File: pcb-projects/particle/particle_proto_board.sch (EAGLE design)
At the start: 37 parts, among them IC1 ATTINY20-SOIC-14S1, IC2 DMC2400UV-SOT563, IC3 DMC2400UV-SOT563

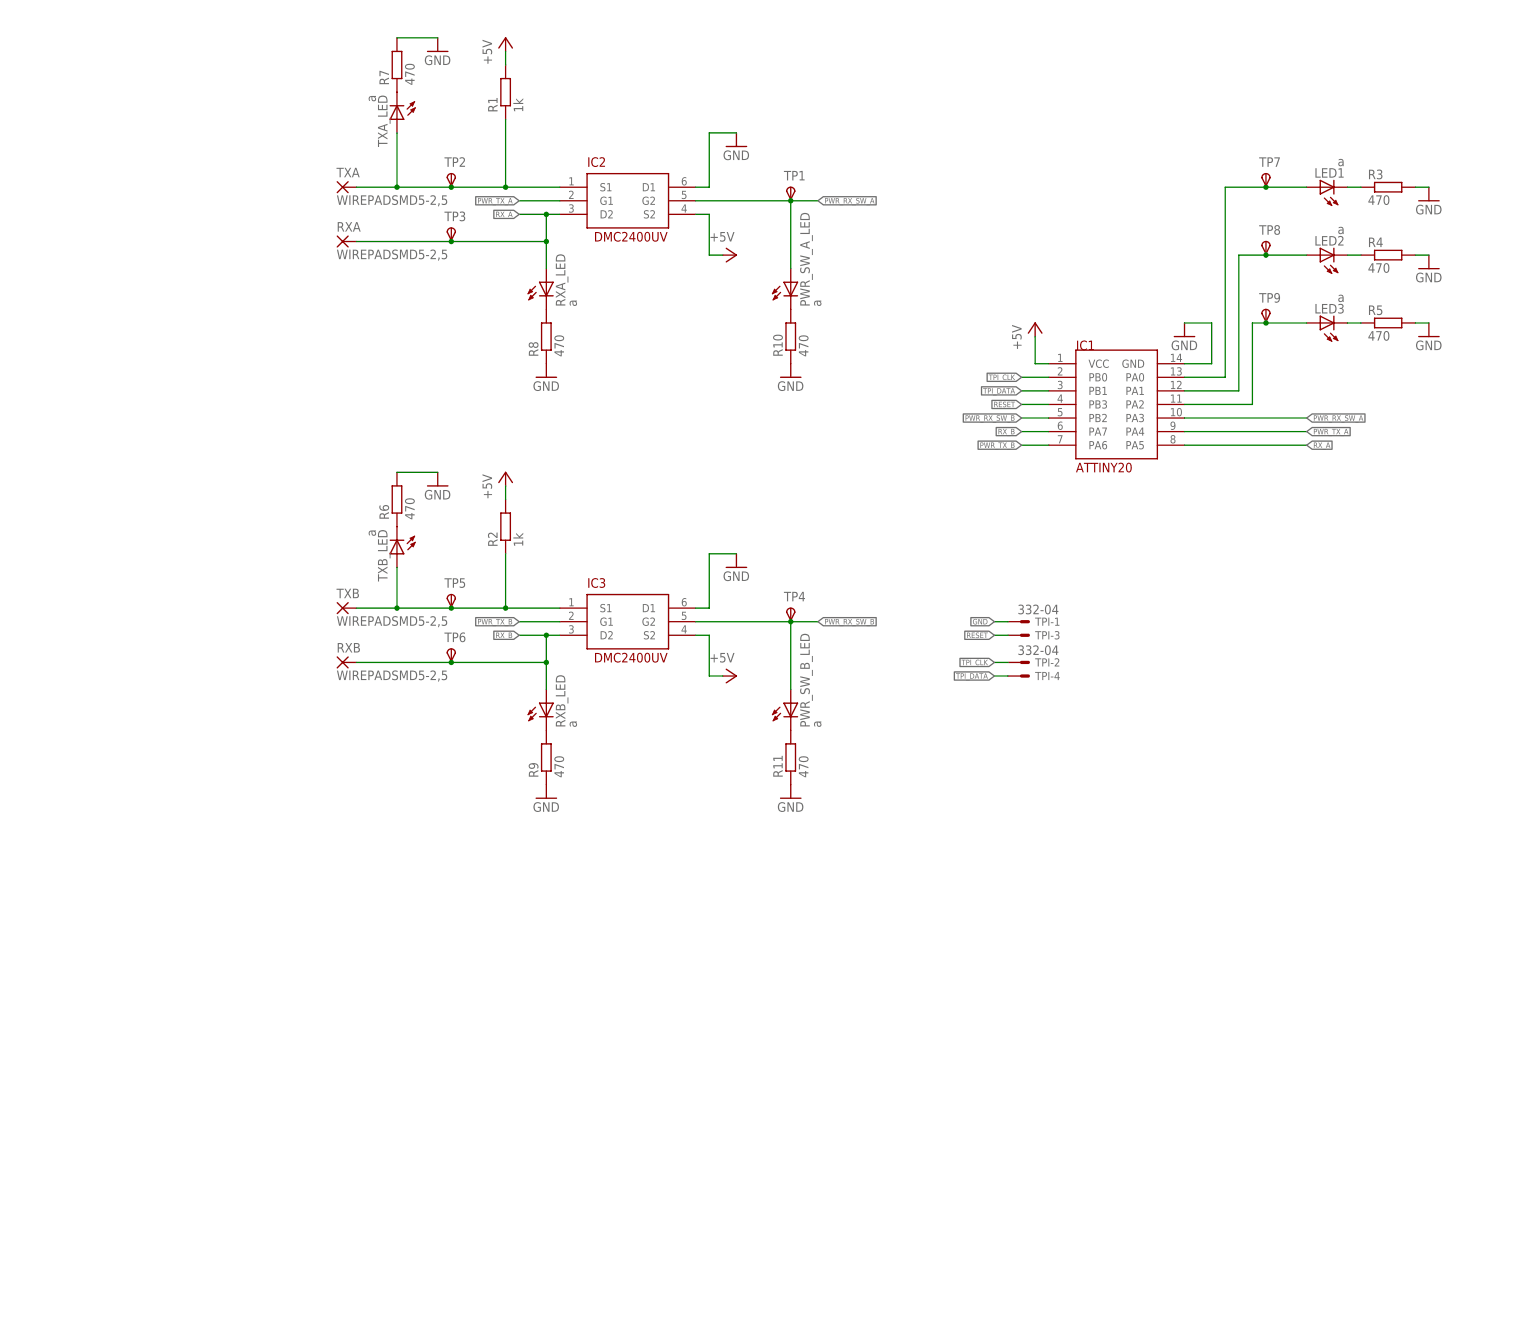
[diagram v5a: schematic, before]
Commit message: replaced packages/library of attiny20 and dmc2400uv
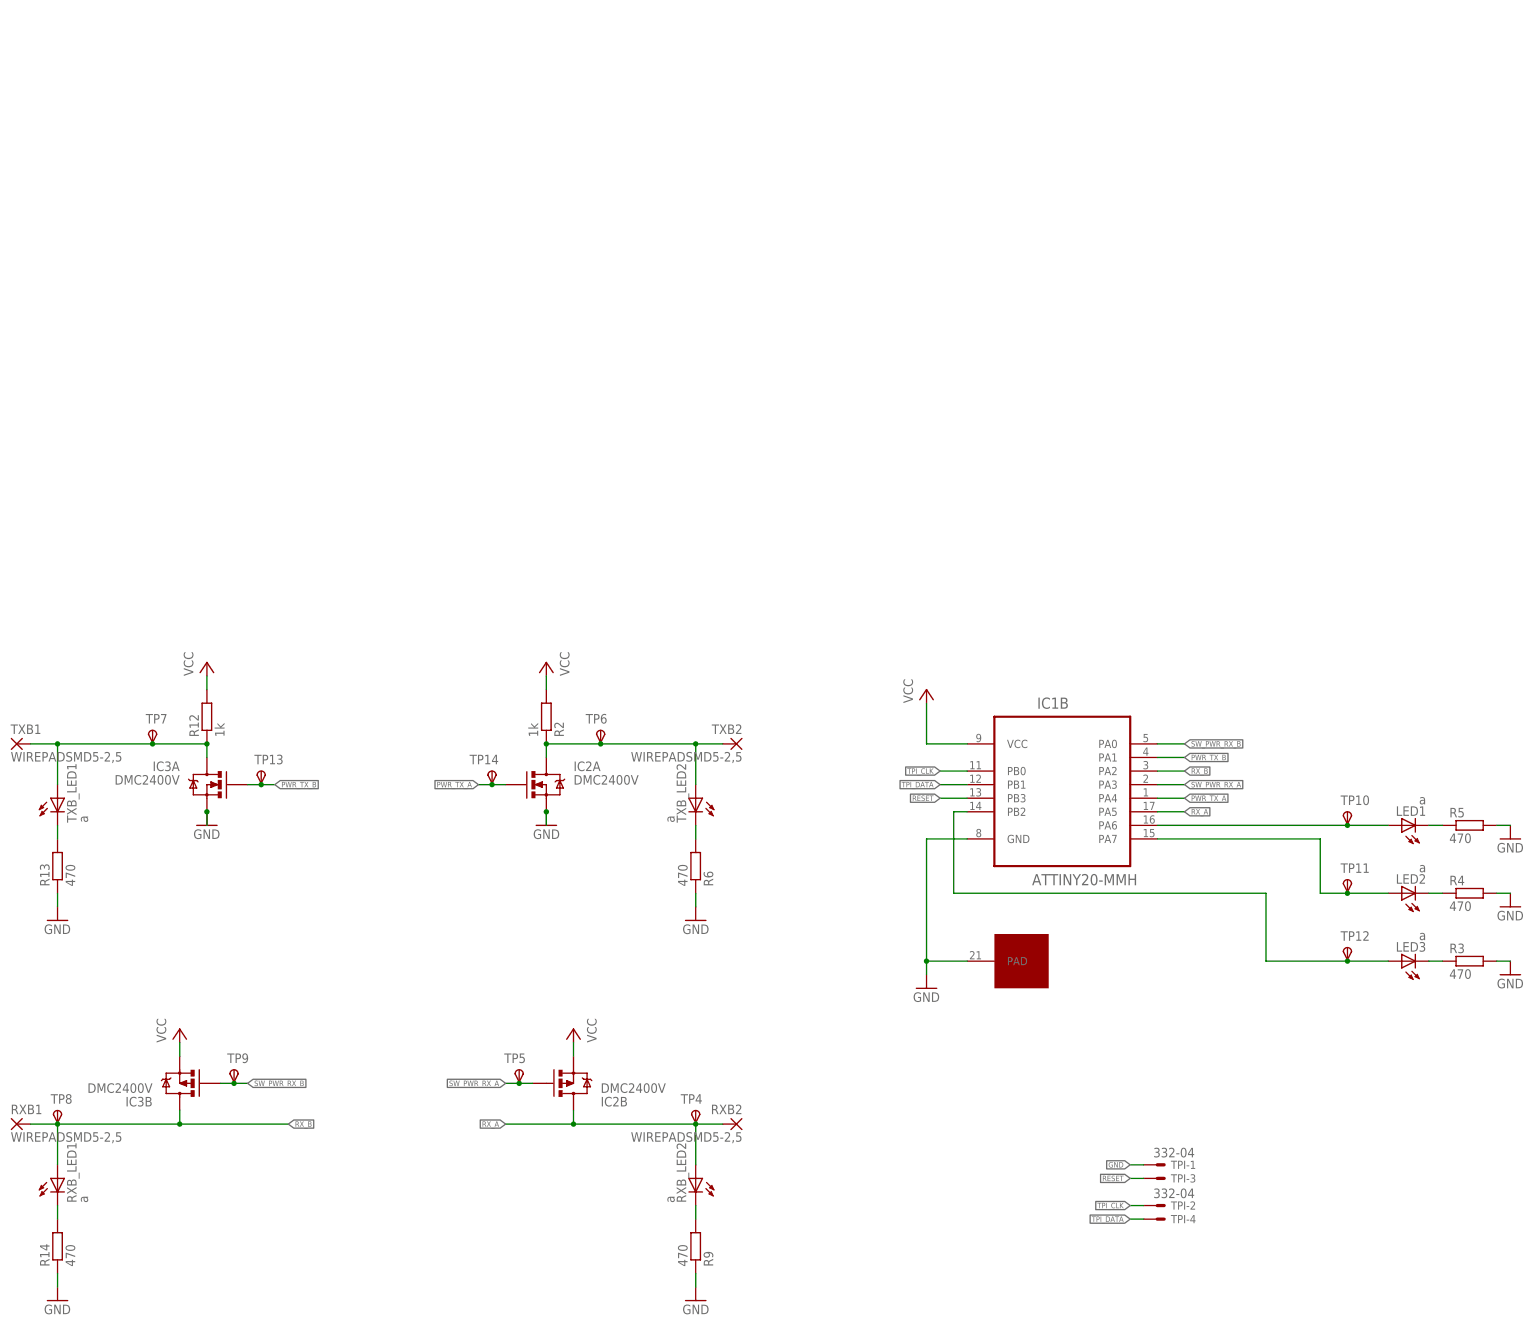
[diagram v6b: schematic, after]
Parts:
- removed PWR_SW_A_LED, PWR_SW_B_LED, RXA_LED, RXB_LED, TXA_LED, TXB_LED: a, led:LEDSML1206
- removed R1: 1k, rcl:R-EU_R1210
- removed R10, R11, R7, R8: 470, rcl:R-EU_R1210
- removed RXA, RXB, TXA, TXB: WIREPADSMD5-2,5, wirepad:WIREPADSMD5-2,5
- removed TP1, TP2, TP3: TPSPAD1-13, testpad:TPSPAD1-13
- added R12: 1k, rcl:R-EU_R1210
- added R13, R14: 470, rcl:R-EU_R1210
- added RXB1, RXB2, TXB1, TXB2: WIREPADSMD5-2,5, wirepad:WIREPADSMD5-2,5
- added RXB_LED1, RXB_LED2, TXB_LED1, TXB_LED2: a, led:LEDSML1206
- added TP10, TP11, TP12, TP13, TP14: TPSPAD1-13, testpad:TPSPAD1-13
- IC1: value ATTINY20-SOIC-14S1 -> ATTINY20-MMH; device ic-attiny20:ATTINY20-SOIC-14S1 -> tiny_particles_MCU:ATTINY20-MMH
- IC2, IC3: value DMC2400UV-SOT563 -> DMC2400V; device dmc2400uv:DMC2400UV-SOT563 -> diodes:DMC2400V
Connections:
- removed net +5V: IC1.VCC, IC2.S2, IC3.S2, R1.2, R2.2
- removed net N$11: R8.2, RXA_LED.C
- removed net N$12: R9.2, RXB_LED.C
- removed net N$13: PWR_SW_A_LED.C, R10.2
- removed net N$14: PWR_SW_B_LED.C, R11.2
- removed net N$5: R6.1, TXB_LED.C
- removed net N$7: R7.1, TXA_LED.C
- removed net PWR_RX_SW_A: IC1.PA3, IC2.G2, PWR_SW_A_LED.A, TP1.PP
- removed net PWR_RX_SW_B: IC1.PB2, IC3.G2, PWR_SW_B_LED.A, TP4.PP
- removed net PWR_TX_A_A_A: IC2.S1, R1.1, TP2.PP, TXA.P, TXA_LED.A
- removed net TXB: IC3.S1, R2.1, TP5.PP, TXB.P, TXB_LED.A
- new net N$21: IC1B.PA6, LED1.A, TP10.PP
- new net N$22: IC1B.PB2, LED3.A, TP12.PP
- new net N$23: IC1B.PA7, LED2.A, TP11.PP
- new net N$24: LED1.C, R5.1
- new net N$26: LED3.C, R3.1
- new net N$6: R13.2, TXB_LED1.C
- new net SW_PWR_RX_A: IC1B.PA3, IC2B.G, TP5.PP
- new net SW_PWR_RX_B: IC1B.PA0, IC3B.G, TP9.PP
- new net VCC: IC1B.VCC, IC2B.S, IC3B.S, R12.2, R2.2
- net GND: now also IC1A.PAD, IC1B.GND, IC2A.S, IC3A.S, R13.1, R14.1, R6.1; no longer IC1.GND, IC2.D1, IC3.D1, R10.1, R11.1, R6.2, R7.2, R8.1
- net N$1: now also IC3A.D, R12.1, TXB1.P, TXB_LED1.A; no longer IC1.PA0, LED1.A
- net N$2: now also IC2A.D, R2.1, TP6.PP, TXB2.P, TXB_LED2.A; no longer IC1.PA2, LED3.A, TP9.PP
- net N$3: now also R6.2, TXB_LED2.C; no longer IC1.PA1, LED2.A, TP8.PP
- net N$4: now also R9.2, RXB_LED2.C; no longer LED1.C, R3.1
- net N$8: now also R14.2, RXB_LED1.C; no longer LED3.C, R5.1
- net PWR_TX_A: now also IC1B.PA4, IC2A.G, TP14.PP; no longer IC1.PA4, IC2.G1
- net PWR_TX_B: now also IC1B.PA1, IC3A.G, TP13.PP; no longer IC1.PA6, IC3.G1
- net RESET: now also IC1B.PB3; no longer IC1.PB3
- net RX_A: now also IC1B.PA5, IC2B.D, RXB2.P, RXB_LED2.A, TP4.PP; no longer IC1.PA5, IC2.D2, RXA.P, RXA_LED.A, TP3.PP
- net RX_B: now also IC1B.PA2, IC3B.D, RXB1.P, RXB_LED1.A, TP8.PP; no longer IC1.PA7, IC3.D2, RXB.P, RXB_LED.A, TP6.PP
- net TPI_CLK: now also IC1B.PB0; no longer IC1.PB0
- net TPI_DATA: now also IC1B.PB1; no longer IC1.PB1
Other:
- moved on the sheet: LED1, LED2, LED3, R2, R3, R4, R5, R6, R9, TP4, TP5, TP6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

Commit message: close 21, close 22
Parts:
- added SPI: 332-06, con-garry:332-06
- TPI: value 332-04 -> 332-06; device con-garry:332-04 -> con-garry:332-06
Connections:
- removed net N$22: IC1B.PB2, LED3.A, TP12.PP
- removed net N$23: IC1B.PA7, LED2.A, TP11.PP
- removed net TPI_DATA: IC1B.PB1, TPI-4.S
- new net MISO: IC1B.PB2, LED3.A, SPI-1.S, TP12.PP
- new net SCK: IC1B.PA7, LED2.A, SPI-3.S, TP11.PP
- new net TPI_DATA/MOSI: IC1B.PB1, SPI-4.S, TPI-1.S
- net GND: now also SPI-6.S, TPI-4.S, TPI-6.S; no longer TPI-1.S
- net RESET: now also SPI-5.S, TPI-5.S; no longer TPI-3.S
- net TPI_CLK: now also TPI-3.S; no longer TPI-2.S
- net VCC: now also SPI-2.S, TPI-2.S
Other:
- moved on the sheet: TPI-1, TPI-2, TPI-3, TPI-4
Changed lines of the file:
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@@
 </classes>
 <parts>
-<part name="TPI" library="con-garry" deviceset="332-04" device=""/>
 <part name="IC1" library="tiny_particles_MCU" deviceset="ATTINY20-MMH" device=""/>
 <part name="GND13" library="supply1" deviceset="GND" device=""/>
@@
 <part name="TP6" library="testpad" deviceset="TPS" device="PAD1-13"/>
 <part name="TP14" library="testpad" deviceset="TPS" device="PAD1-13"/>
+<part name="TPI" library="con-garry" deviceset="332-06" device=""/>
+<part name="SPI" library="con-garry" deviceset="332-06" device=""/>
 </parts>
 <sheets>
@@
 </plain>
 <instances>
-<instance part="TPI" gate="-1" x="99.06" y="-58.42"/>
-<instance part="TPI" gate="-2" x="99.06" y="-66.04"/>
-<instance part="TPI" gate="-3" x="99.06" y="-60.96"/>
-<instance part="TPI" gate="-4" x="99.06" y="-68.58"/>
 <instance part="IC1" gate="B" x="81.28" y="15.24"/>
 <instance part="IC1" gate="A" x="66.04" y="-20.32"/>
@@
 <instance part="TP6" gate="G$1" x="-5.08" y="22.86" rot="MR0"/>
 <instance part="TP14" gate="G$1" x="-25.4" y="15.24" rot="MR0"/>
+<instance part="TPI" gate="-1" x="73.66" y="-53.34"/>
+<instance part="TPI" gate="-2" x="73.66" y="-63.5"/>
+<instance part="TPI" gate="-3" x="73.66" y="-55.88"/>
+<instance part="TPI" gate="-4" x="73.66" y="-66.04"/>
+<instance part="TPI" gate="-5" x="73.66" y="-58.42"/>
+<instance part="TPI" gate="-6" x="73.66" y="-68.58"/>
+<instance part="SPI" gate="-1" x="124.46" y="-53.34"/>
+<instance part="SPI" gate="-2" x="124.46" y="-63.5"/>
+<instance part="SPI" gate="-3" x="124.46" y="-55.88"/>
+<instance part="SPI" gate="-4" x="124.46" y="-66.04"/>
+<instance part="SPI" gate="-5" x="124.46" y="-58.42"/>
+<instance part="SPI" gate="-6" x="124.46" y="-68.58"/>
 </instances>
 <busses>
@@
 <nets>
 <net name="GND" class="0">
-<segment>
-<pinref part="TPI" gate="-1" pin="S"/>
-<wire x1="96.52" y1="-58.42" x2="93.98" y2="-58.42" width="0.1524" layer="91"/>
-<label x="93.98" y="-58.42" size="1.016" layer="95" rot="R180" xref="yes"/>
-</segment>
 <segment>
 <pinref part="IC1" gate="B" pin="GND"/>
@@
 <wire x1="12.7" y1="-81.28" x2="12.7" y2="-78.74" width="0.1524" layer="91"/>
 </segment>
+<segment>
+<pinref part="TPI" gate="-6" pin="S"/>
+<wire x1="71.12" y1="-68.58" x2="68.58" y2="-68.58" width="0.1524" layer="91"/>
+<label x="68.58" y="-68.58" size="1.016" layer="95" rot="R180" xref="yes"/>
+</segment>
+<segment>
+<pinref part="SPI" gate="-6" pin="S"/>
+<wire x1="121.92" y1="-68.58" x2="119.38" y2="-68.58" width="0.1524" layer="91"/>
+<label x="119.38" y="-68.58" size="1.016" layer="95" rot="R180" xref="yes"/>
+</segment>
+<segment>
+<pinref part="TPI" gate="-4" pin="S"/>
+<wire x1="71.12" y1="-66.04" x2="68.58" y2="-66.04" width="0.1524" layer="91"/>
+<label x="68.58" y="-66.04" size="1.016" layer="95" rot="R180" xref="yes"/>
+</segment>
 </net>
 <net name="TPI_CLK" class="0">
@@
 </segment>
 <segment>
-<pinref part="TPI" gate="-2" pin="S"/>
-<wire x1="96.52" y1="-66.04" x2="93.98" y2="-66.04" width="0.1524" layer="91"/>
-<label x="93.98" y="-66.04" size="1.016" layer="95" rot="R180" xref="yes"/>
+<pinref part="TPI" gate="-3" pin="S"/>
+<wire x1="71.12" y1="-55.88" x2="68.58" y2="-55.88" width="0.1524" layer="91"/>
+<label x="68.58" y="-55.88" size="1.016" layer="95" rot="R180" xref="yes"/>
 </segment>
 </net>
@@
 </segment>
 </net>
-<net name="TPI_DATA" class="0">
-<segment>
-<pinref part="TPI" gate="-4" pin="S"/>
-<wire x1="96.52" y1="-68.58" x2="93.98" y2="-68.58" width="0.1524" layer="91"/>
-<label x="93.98" y="-68.58" size="1.016" layer="95" rot="R180" xref="yes"/>
-</segment>
+<net name="TPI_DATA/MOSI" class="0">
 <segment>
 <wire x1="63.5" y1="12.7" x2="58.42" y2="12.7" width="0.1524" layer="91"/>
@@
 <pinref part="IC1" gate="B" pin="PB1"/>
 </segment>
+<segment>
+<pinref part="TPI" gate="-1" pin="S"/>
+<wire x1="71.12" y1="-53.34" x2="68.58" y2="-53.34" width="0.1524" layer="91"/>
+<label x="68.58" y="-53.34" size="1.016" layer="95" rot="R180" xref="yes"/>
+</segment>
+<segment>
+<pinref part="SPI" gate="-4" pin="S"/>
+<wire x1="121.92" y1="-66.04" x2="119.38" y2="-66.04" width="0.1524" layer="91"/>
+<label x="119.38" y="-66.04" size="1.016" layer="95" rot="R180" xref="yes"/>
+</segment>
 </net>
 <net name="RESET" class="0">
-<segment>
-<pinref part="TPI" gate="-3" pin="S"/>
-<wire x1="96.52" y1="-60.96" x2="93.98" y2="-60.96" width="0.1524" layer="91"/>
-<label x="93.98" y="-60.96" size="1.016" layer="95" rot="R180" xref="yes"/>
-</segment>
 <segment>
 <wire x1="63.5" y1="10.16" x2="58.42" y2="10.16" width="0.1524" layer="91"/>
 <label x="58.42" y="10.16" size="1.016" layer="95" rot="R180" xref="yes"/>
 <pinref part="IC1" gate="B" pin="PB3"/>
+</segment>
+<segment>
+<pinref part="TPI" gate="-5" pin="S"/>
+<wire x1="71.12" y1="-58.42" x2="68.58" y2="-58.42" width="0.1524" layer="91"/>
+<label x="68.58" y="-58.42" size="1.016" layer="95" rot="R180" xref="yes"/>
+</segment>
+<segment>
+<pinref part="SPI" gate="-5" pin="S"/>
+<wire x1="121.92" y1="-58.42" x2="119.38" y2="-58.42" width="0.1524" layer="91"/>
+<label x="119.38" y="-58.42" size="1.016" layer="95" rot="R180" xref="yes"/>
 </segment>
 </net>
@@
 </segment>
 </net>
-<net name="N$22" class="0">
-<segment>
-<wire x1="119.38" y1="-7.62" x2="119.38" y2="-20.32" width="0.1524" layer="91"/>
+<net name="MISO" class="0">
+<segment>
+<wire x1="99.06" y1="-7.62" x2="99.06" y2="-20.32" width="0.1524" layer="91"/>
 <pinref part="IC1" gate="B" pin="PB2"/>
 <wire x1="63.5" y1="7.62" x2="60.96" y2="7.62" width="0.1524" layer="91"/>
 <wire x1="60.96" y1="7.62" x2="60.96" y2="-7.62" width="0.1524" layer="91"/>
-<wire x1="60.96" y1="-7.62" x2="119.38" y2="-7.62" width="0.1524" layer="91"/>
+<wire x1="60.96" y1="-7.62" x2="99.06" y2="-7.62" width="0.1524" layer="91"/>
 <pinref part="LED3" gate="G$1" pin="A"/>
-<wire x1="119.38" y1="-20.32" x2="134.62" y2="-20.32" width="0.1524" layer="91"/>
+<wire x1="99.06" y1="-20.32" x2="134.62" y2="-20.32" width="0.1524" layer="91"/>
 <pinref part="TP12" gate="G$1" pin="PP"/>
 <junction x="134.62" y="-20.32"/>
 <wire x1="134.62" y1="-20.32" x2="142.24" y2="-20.32" width="0.1524" layer="91"/>
-</segment>
-</net>
-<net name="N$23" class="0">
+<label x="58.42" y="7.62" size="1.016" layer="95" rot="R180" xref="yes"/>
+<wire x1="58.42" y1="7.62" x2="60.96" y2="7.62" width="0.1524" layer="91"/>
+<junction x="60.96" y="7.62"/>
+</segment>
+<segment>
+<pinref part="SPI" gate="-1" pin="S"/>
+<wire x1="121.92" y1="-53.34" x2="119.38" y2="-53.34" width="0.1524" layer="91"/>
+<label x="119.38" y="-53.34" size="1.016" layer="95" rot="R180" xref="yes"/>
+</segment>
+</net>
+<net name="SCK" class="0">
 <segment>
 <pinref part="LED2" gate="G$1" pin="A"/>
-<wire x1="129.54" y1="-7.62" x2="134.62" y2="-7.62" width="0.1524" layer="91"/>
+<wire x1="104.14" y1="-7.62" x2="134.62" y2="-7.62" width="0.1524" layer="91"/>
 <pinref part="TP11" gate="G$1" pin="PP"/>
 <wire x1="134.62" y1="-7.62" x2="142.24" y2="-7.62" width="0.1524" layer="91"/>
 <junction x="134.62" y="-7.62"/>
 <pinref part="IC1" gate="B" pin="PA7"/>
-<wire x1="99.06" y1="2.54" x2="129.54" y2="2.54" width="0.1524" layer="91"/>
-<wire x1="129.54" y1="2.54" x2="129.54" y2="-7.62" width="0.1524" layer="91"/>
+<wire x1="99.06" y1="2.54" x2="104.14" y2="2.54" width="0.1524" layer="91"/>
+<wire x1="104.14" y1="2.54" x2="104.14" y2="-7.62" width="0.1524" layer="91"/>
+<label x="104.14" y="2.54" size="1.016" layer="95" xref="yes"/>
+</segment>
+<segment>
+<pinref part="SPI" gate="-3" pin="S"/>
+<wire x1="121.92" y1="-55.88" x2="119.38" y2="-55.88" width="0.1524" layer="91"/>
+<label x="119.38" y="-55.88" size="1.016" layer="95" rot="R180" xref="yes"/>
 </segment>
 </net>
@@
 <wire x1="-10.16" y1="-38.1" x2="-10.16" y2="-35.56" width="0.1524" layer="91"/>
 </segment>
-</net>
+<segment>
+<pinref part="TPI" gate="-2" pin="S"/>
+<wire x1="71.12" y1="-63.5" x2="68.58" y2="-63.5" width="0.1524" layer="91"/>
+<label x="68.58" y="-63.5" size="1.016" layer="95" rot="R180" xref="yes"/>
+</segment>
+<segment>
+<pinref part="SPI" gate="-2" pin="S"/>
+<wire x1="121.92" y1="-63.5" x2="119.38" y2="-63.5" width="0.1524" layer="91"/>
+<label x="119.38" y="-63.5" size="1.016" layer="95" rot="R180" xref="yes"/>
+</segment>
+</net>
